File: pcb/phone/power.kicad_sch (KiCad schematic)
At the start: 28 parts, among them CN1 S2B-PH-SM4-TB, SW21 SSSS811101, U10 MAX17048G+T10, U11 MCP73831-2ACI/MC, U8 TPS63021DSJR, U9 TPS7A0218PDBVR

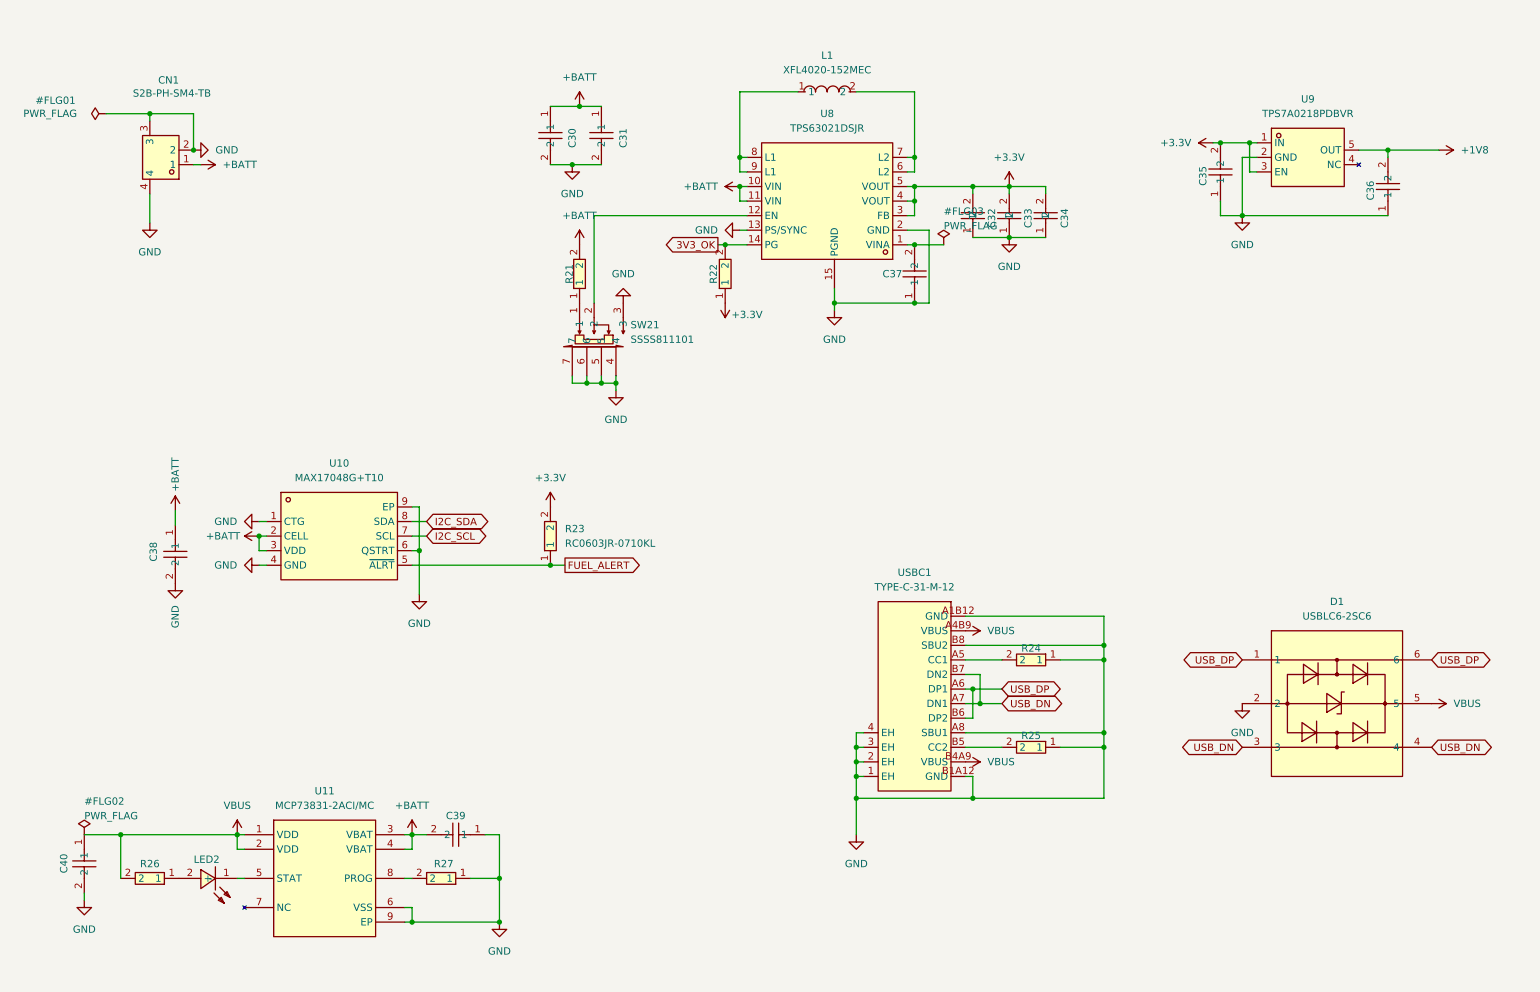
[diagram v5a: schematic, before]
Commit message: Pivot form factor to candybar/single-board + doc-audit fixes
Flip/clamshell (two PCBs + hinge flex) → candybar (single PCB). Drops
outer display, hinge flex connectors (J8/J9), daughterboard. Display
mounts directly via J7 ZIF. Backlight FET architecture conflict resolved
(FET on single board). See project-log.md 2026-08-16.

Doc-audit caught 4 stale references the pivot session missed:
- datasheets/README.md: ST7789V.pdf desc, ER-TFT1.14-2 row, outer display
  raw panel line — all marked DROPPED
- ic-by-ic-review.md: ST7789 outer display row + Display_Daughter sheet
  reference — marked DROPPED

KiCad: modem/phone/power sheets + PCB updated for single-board design.

Generated with [Devin](https://devin.ai)

Co-Authored-By: Devin <158243242+devin-ai-integration[bot]@users.noreply.github.com>
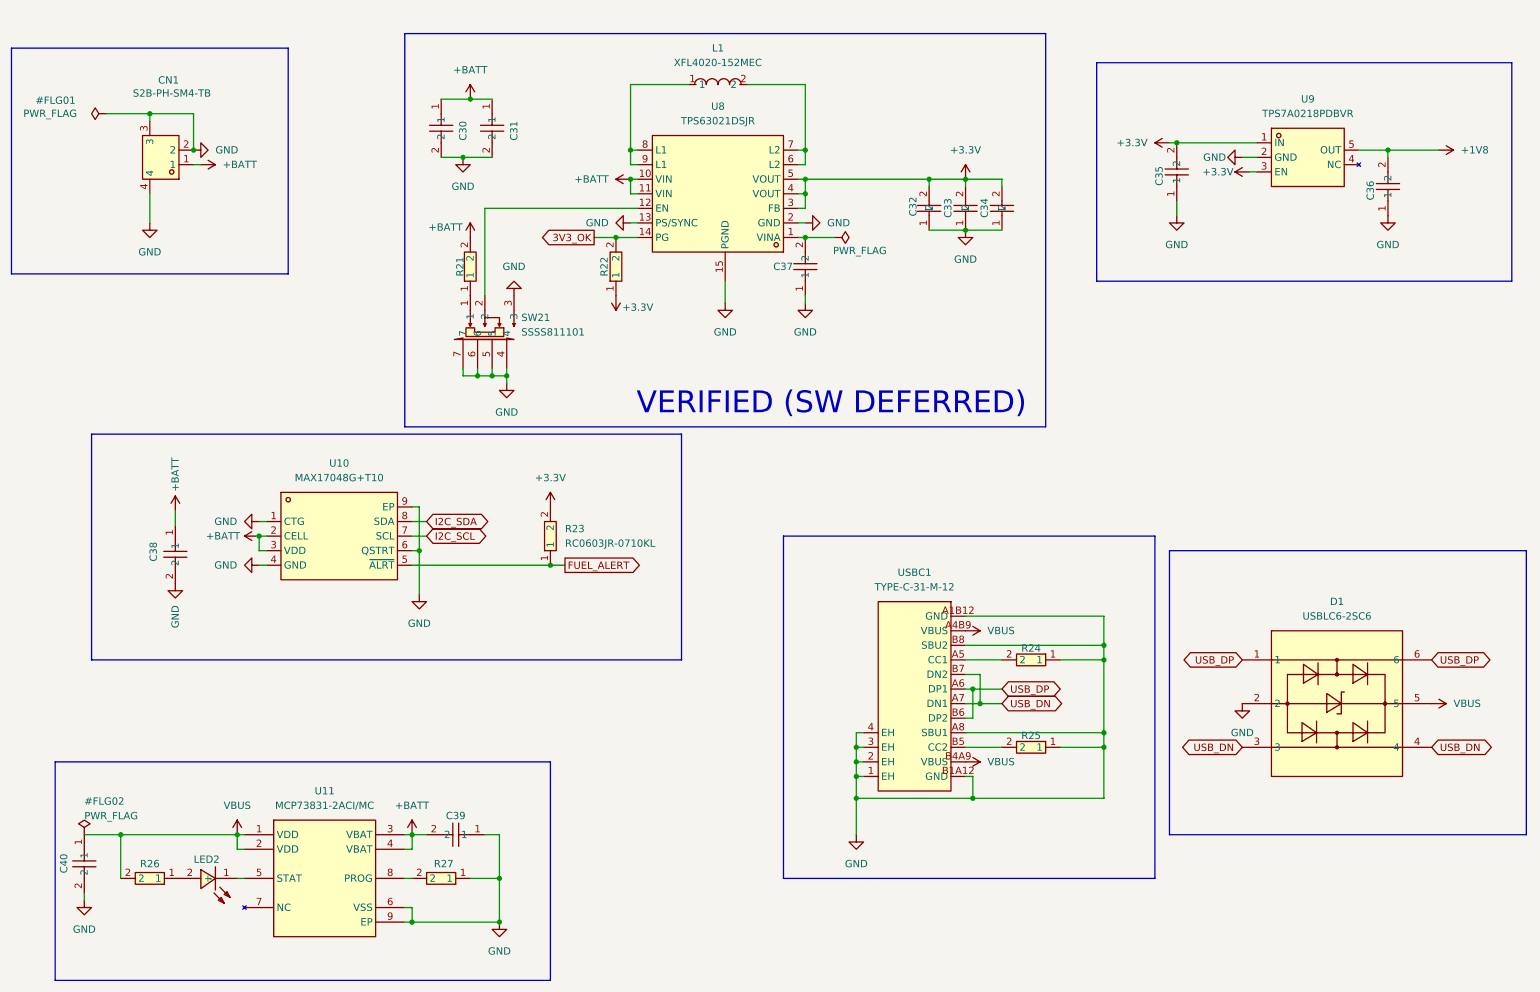
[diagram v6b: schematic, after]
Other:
- note added: "VERIFIED (SW DEFERRED)"
- moved on the sheet: C30, C31, C32, C33, C34, C35, C37, L1, R21, R22, SW21, U8

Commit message: Restructure display sheet for candybar + fix pinout + add backlight FET + power switch reversal
Display sheet (LOCKED):
- Fix J_DISP1 pinout to match HS20HS072RX datasheet (was 1/12 correct, now all 14 pins match)
- Add backlight FET circuit: Q1 (AO3400A), R20 (100ohm gate), R5 (10k pulldown), R19 moved to pin 10
- Fix R19 MPN: was 470ohm part with 4.7ohm value, swapped to RC0603JR-074R7L (correct 4.7ohm)
- Move display power from +1V8 to +3.3V (1.8V below VCC min 2.4V)
- Remove display_daughter sheet entry, J_HINGE1, J_HINGE2, OUTER_CS/OUTER_DC
- Add no-connect flags on MCU PG9/PG10 (freed from outer display)
- FPC connector orientation review flagged for PCB layout phase

Power switch (reversed 2026-08-27):
- Move SW21 from battery path back to TPS63021 EN pin (signal-level)
- Select C&K OS102011MA1QN1 (100mA SPDT, LCSC C226259), 8.4mm actuator, usable as finger toggle
- Battery always connected, charging while off restored
- Supersedes 2026-08-17 battery-path architecture

New library parts:
- ics:AO3400A (N-ch MOSFET, SOT-23, LCSC C20917)
- passives:0603WAF1000T5E (100ohm 0603, LCSC C22775)
- passives:RC0603JR-074R7L (4.7ohm 0603, LCSC C137621)
- electromech:OS102011MA1QN1 (SPDT slide switch, LCSC C226259)

Docs updated:
- project-log: 3 new entries (display review, power switch reversal, USB hub)
- bom.md: item 25b switch selected, display backlight parts
- block-diagram.md: +BATT net (no switch), U8 EN pin (switched by SW21)
- schematic-completion-plan.md: display sheet LOCKED, section F complete
- task-tracker.md: O2 updated with 2026-08-27 architecture
- ic-by-ic-review.md: Q3 superseded again, DEF-001 updated
- datasheets/README.md: HS20HS072RX pinout verified, SPI confirmed

Generated with [Devin](https://devin.ai)

Co-Authored-By: Devin <158243242+devin-ai-integration[bot]@users.noreply.github.com>
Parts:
- removed SW21: SSSS811101, easyeda2kicad:SW-SMD_SSSS811101, symbol electromech:SSSS811101
- added SW21: OS102011MA1QN1, easyeda2kicad:SW-TH_OS102011MA1QN1, symbol electromech:OS102011MA1QN1
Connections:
- net GND: now also SW21.3, SW21.4, SW21.5
- net at R21.1: now also SW21.1
- net at U8.12 (EN): now also SW21.2
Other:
- note added: "LOCKED 8/16 MD"
- note added: "LOCKED 8/29 MD"
- note removed: "VERIFIED (SW DEFERRED)"
